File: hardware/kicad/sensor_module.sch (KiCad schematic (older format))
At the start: 31 parts, among them P1 CONN_01X04, P2 PH_Sensor, P3 Moisture_Sensor, U0 STLM75M2F, U1 TCA9543ADR, U2 TSL2550D, U3 HIH7121, U4 MCP3422A0-E/SN

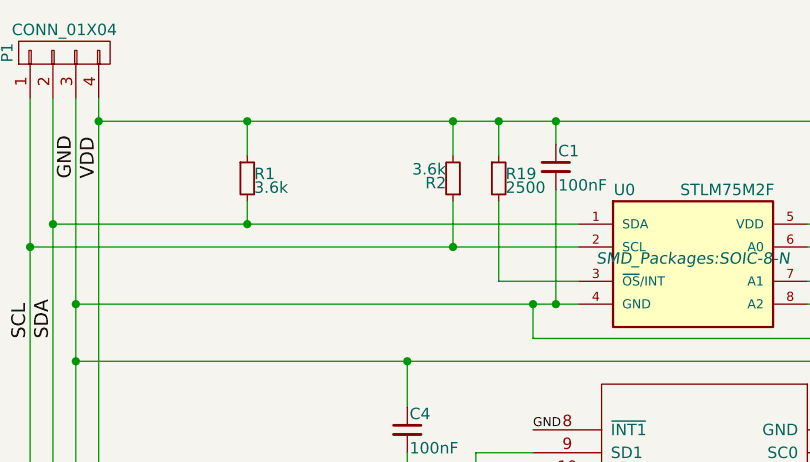
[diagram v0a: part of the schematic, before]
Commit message: Close #2: Implemented Humidity Sensor Module
The humidity sensor is working properly and currently measuring ambient
humidity.

It has a feature that will measure temperature as well. I intend to use
this feature to verify that the device is working properly and if it's
accurate enough, I may remove the dedicated temperature sensor.
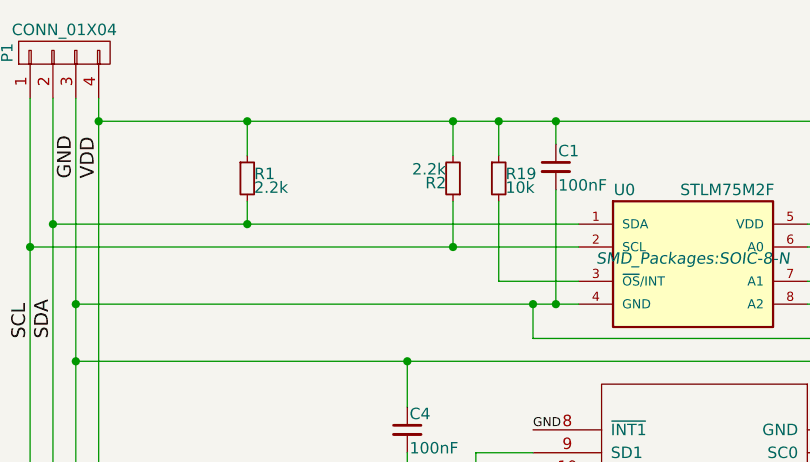
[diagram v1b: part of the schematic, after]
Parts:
- R1, R2: value 3.6k -> 2.2k
- R19: value 2500 -> 10k
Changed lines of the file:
@@
 P 2050 1550
 F 0 "R1" H 2080 1570 50  0000 L CNN
-F 1 "3.6k" H 2080 1510 50  0000 L CNN
+F 1 "2.2k" H 2080 1510 50  0000 L CNN
 F 2 "Resistors_SMD:R_0201" H 2050 1550 50  0001 C CNN
 F 3 "" H 2050 1550 50  0000 C CNN
@@
 P 2950 1550
 F 0 "R2" H 2980 1570 50  0000 L CNN
-F 1 "3.6k" H 2980 1510 50  0000 L CNN
+F 1 "2.2k" H 2980 1510 50  0000 L CNN
 F 2 "Resistors_SMD:R_0201" H 2950 1550 50  0001 C CNN
 F 3 "" H 2950 1550 50  0000 C CNN
@@
 P 3150 1550
 F 0 "R19" H 3180 1570 50  0000 L CNN
-F 1 "2500" H 3180 1510 50  0000 L CNN
+F 1 "10k" H 3180 1510 50  0000 L CNN
 F 2 "Resistors_SMD:R_0201" H 3150 1550 50  0001 C CNN
 F 3 "" H 3150 1550 50  0000 C CNN

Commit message: Restructured Sensor Model
This new sensor model structure hides each sensor cluster behind a
single node head (in this case, the node head is an I2C multiplexer).
This eliminates the need for individual sensor addresses and further
generalizes the models. This also abstracts more hardware away from the
python script and thus will make it easier for a user to add sensors.
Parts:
- P1: symbol CONN_01X04 -> CONN_01X04-RESCUE-sensor_module
- P3: symbol CONN_01X03 -> CONN_01X03-RESCUE-sensor_module
- U1: symbol TCA9543ADR -> TCA9543ADR-RESCUE-sensor_module
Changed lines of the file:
@@
 EESchema Schematic File Version 2
+LIBS:sensor_module-rescue
 LIBS:power
 LIBS:device
@@
 $EndDescr
 $Comp
-L CONN_01X04 P1
+L CONN_01X04-RESCUE-sensor_module P1
 U 1 1 56A04587
 P 1250 1000
@@
 $EndComp
 $Comp
-L TCA9543ADR U1
+L TCA9543ADR-RESCUE-sensor_module U1
 U 1 1 56A2F2CE
 P 4050 2950
@@
 $EndComp
 $Comp
-L CONN_01X03 P3
+L CONN_01X03-RESCUE-sensor_module P3
 U 1 1 56A56595
 P 5700 5000
